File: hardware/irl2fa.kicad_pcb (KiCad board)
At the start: 2 copper layers, 80 x 34 mm, 52 parts, among them J1 FH34SRJ-24S, J3 TC2030-NL, Q1 AO3401A, Q2 AO3401A, Q3 Si1308EDL, Q4 AO3400A, Q5 VEMT2523SLX01, SW1 SKRHABE010, U1 STM32U083KCU6, U2 RV-3032-C7

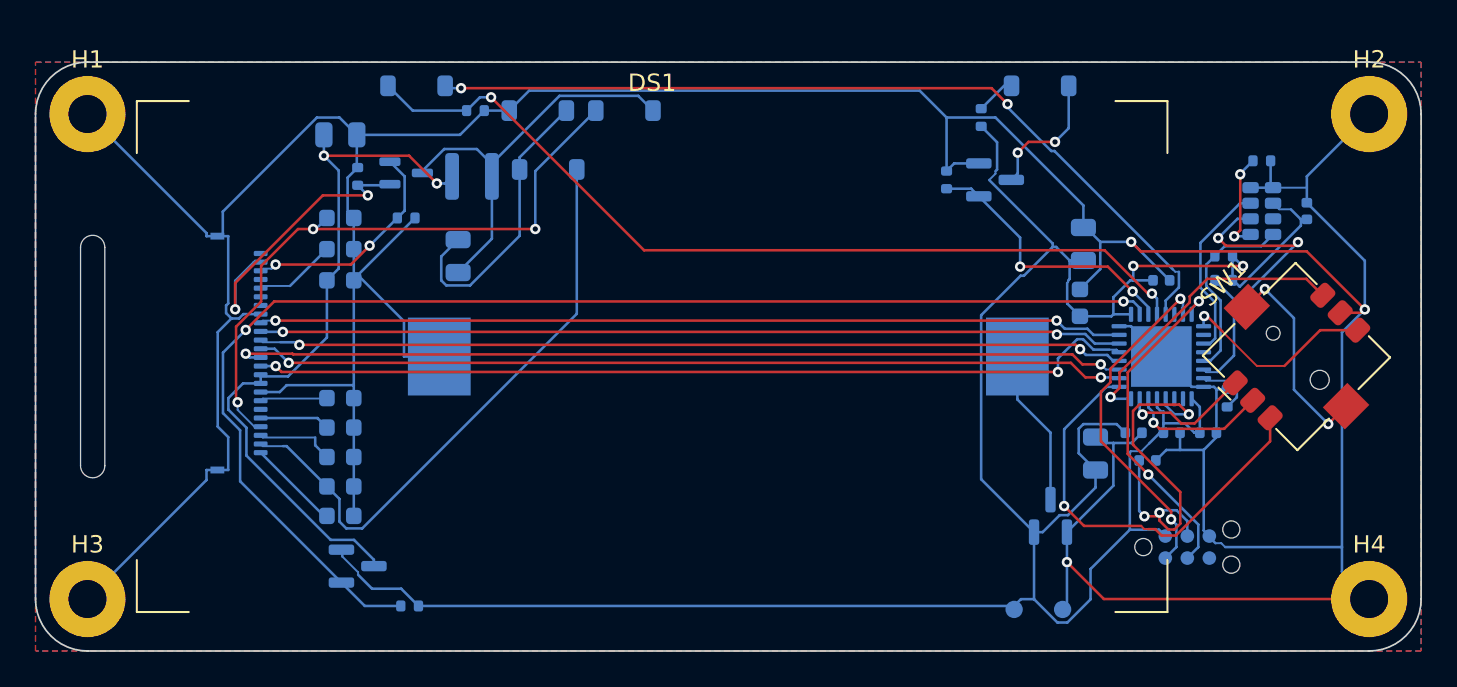
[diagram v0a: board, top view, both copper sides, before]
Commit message: Make the fob smaller: 80.9 x 34.9 x 11.0 mm case, 77 x 31 x 0.8 mm board
The 7.5 mm BS-24-B4AA016 holder set the case thickness. Replace it with
the MYOUNG MY-2450-01 CR2450 clip (LCSC C964845, 5.70 mm, 5355 in stock,
$0.17): a sprung plate over the cell, with a bare 12 mm ENIG pad under
it as the negative contact. Same cell, so the battery-life budget is
unchanged.

- Board 80 x 34 x 1.0 -> 77 x 31 x 0.8 mm, corner radius 2.6, holes at
  the corner centres. Glass 0.9 mm from the long edges, 0.4 mm clear of
  the case's screw bosses; joystick 1.2 mm from the glass.
- Case 83.9 x 37.9 x 13.0 -> 80.9 x 34.9 x 11.0 mm (keep-out 7.6 -> 5.8).
- New footprint and model for the clip, drawn from drawing MY-CP-0106.
  The courtyard is the union of plate, cell and pads. The SKRH courtyard
  now follows body and pads instead of their bounding box.
- The cell slides in from the bottom edge. Rule area: no vias under the
  cell. J1 keeps its FPC insertion offset on the thinner board.
- Re-placed and re-routed (Freerouting 2.5): ERC/DRC 0 errors,
  0 unconnected. Fab outputs, case STL/3MF, renders and docs regenerated.
- Case tests take the skin samples above and below the window from
  board.yaml rather than fixed coordinates.

Co-Authored-By: Claude Opus 5.5 <noreply@anthropic.com>
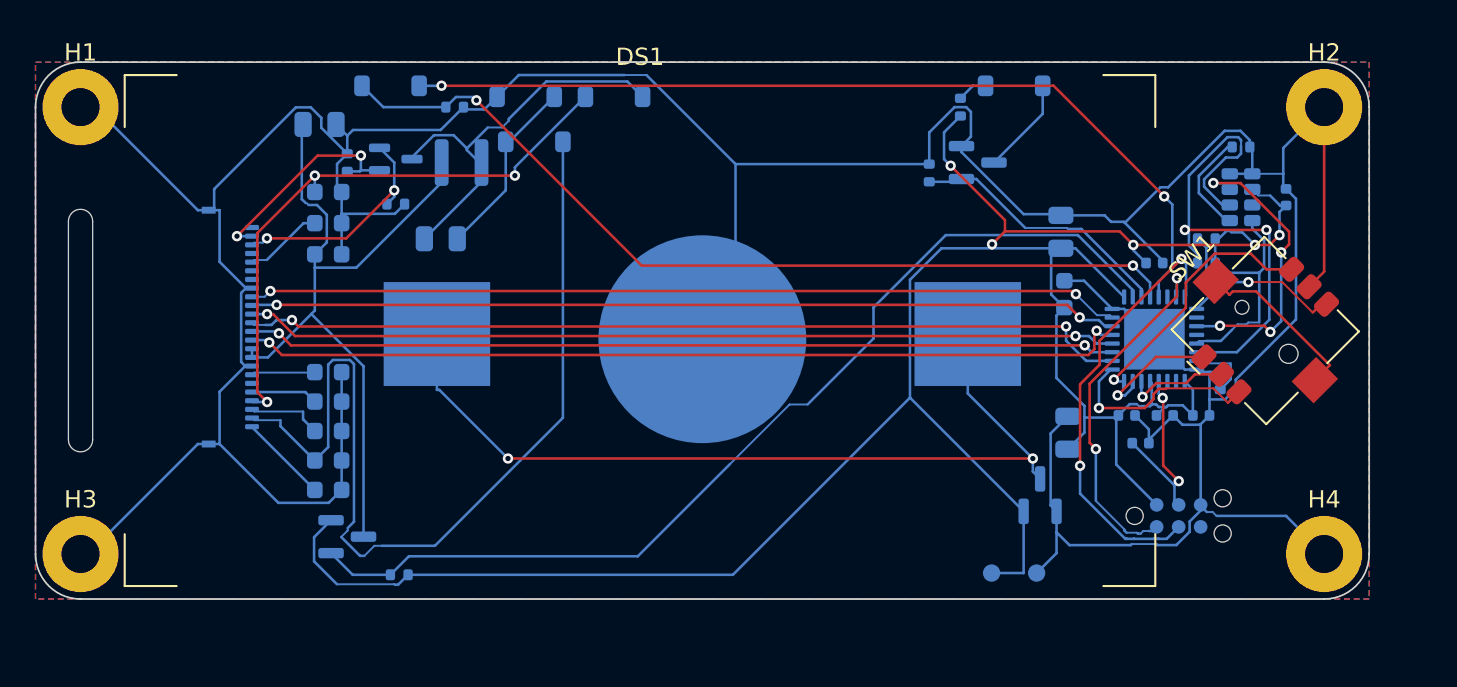
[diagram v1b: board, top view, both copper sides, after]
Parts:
- BT1: footprint irl2fa:BatteryHolder_MYOUNG_BS-24-B4AA016_CR2450 -> irl2fa:BatteryHolder_MYOUNG_MY-2450-01_CR2450
- moved H4 3.68 mm to (174.4, 128.4)
- moved H2 2.63 mm to (174.4, 102.6)
- moved H3 2.63 mm to (102.6, 128.4)
- moved TP2 2.58 mm to (157.8, 129.5)
- moved TP1 2.47 mm to (155.2, 129.5)
- moved SW1 2.34 mm to (171.0, 115.5)
- moved C2 2.00 mm to (159.6, 121.4)
- moved R5 1.90 mm to (121.0, 129.6)
- moved J3 1.87 mm to (166.0, 126.2)
- moved BT1 1.80 mm to (138.5, 116.0), turned to 180 degrees
- moved Q2 1.80 mm to (118.0, 127.4)
- moved D1 1.79 mm to (128.8, 104.6)
- moved C12 1.66 mm to (116.9, 107.5)
- moved C13 1.66 mm to (116.9, 109.3)
- moved C14 1.66 mm to (116.9, 111.1)
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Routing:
- net /VBAT_RAW: track 9.05 -> 49.4 mm, vias 0 -> 2
- net /GND: track 267.4 -> 246.3 mm, vias 3 -> 0
- net /EPD_PREVGL: track 34.5 -> 55.2 mm
- net /EPD_PWR_N: track 74.8 -> 57.7 mm, vias 2 -> 0
- net /JOY_C: track 24.8 -> 11.9 mm
- net /I2C_SDA: track 19.3 -> 30.3 mm
- net /NRST: track 22.2 -> 11.3 mm, vias 3 -> 2
- net /RTC_INT: track 10.5 -> 17.3 mm, vias 0 -> 4
- net /EPD_NEG: track 16.9 -> 10.6 mm
- net /SWCLK: track 19.4 -> 25.4 mm
- net /EPD_GDR: track 17.6 -> 12.7 mm
- net /I2C_SCL: track 11.1 -> 15.6 mm
- net /VBAT: track 141.0 -> 144.4 mm, vias 2 -> 5
- net /JOY_D: track 11.5 -> 9.07 mm
- net /EPD_PREVGH: track 36.7 -> 34.3 mm
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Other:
- board size 80 x 34 mm -> 77 x 31 mm

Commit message: Fix the silkscreen and turn the IR parts to face out through the top edge
Silkscreen: reference designators overlapped each other, sat on pads and ran
off the board edge, because silk_overlap, silk_over_copper and
silk_edge_clearance were only DRC warnings. They are errors now, and a new
gen_pcb.py --step silk places every label clear of pads, other silk, part
bodies, the coin cell and its insertion path, the FPC slot and the edge
(0.8 mm, 0.65 mm where that can't fit; hidden only where nothing fits: the
display, the booster diodes and inductor, and Q5). R3/R4 moved 0.3 mm clear
of U2's pin-1 mark, the clip's "+" moved to the contact away from C11, and
the IR parts' pin-1 bars stop short of the edge.

IR orientation: placing a part on the back mirrors it top to bottom, so D4
and Q5, placed at 0 deg, had their lenses facing into the board. Their pads
are symmetric, so ERC, DRC and the footprint checks all passed. They are now
at 180 deg (board re-routed, DRC clean), and test_orientation.py checks it.

Also: gen_pcb.py --step refresh (library footprint updates without
re-routing), hardware/tools/render_pcb.sh and `make renders`, new renders.

Co-Authored-By: Claude Opus 5.5 <noreply@anthropic.com>
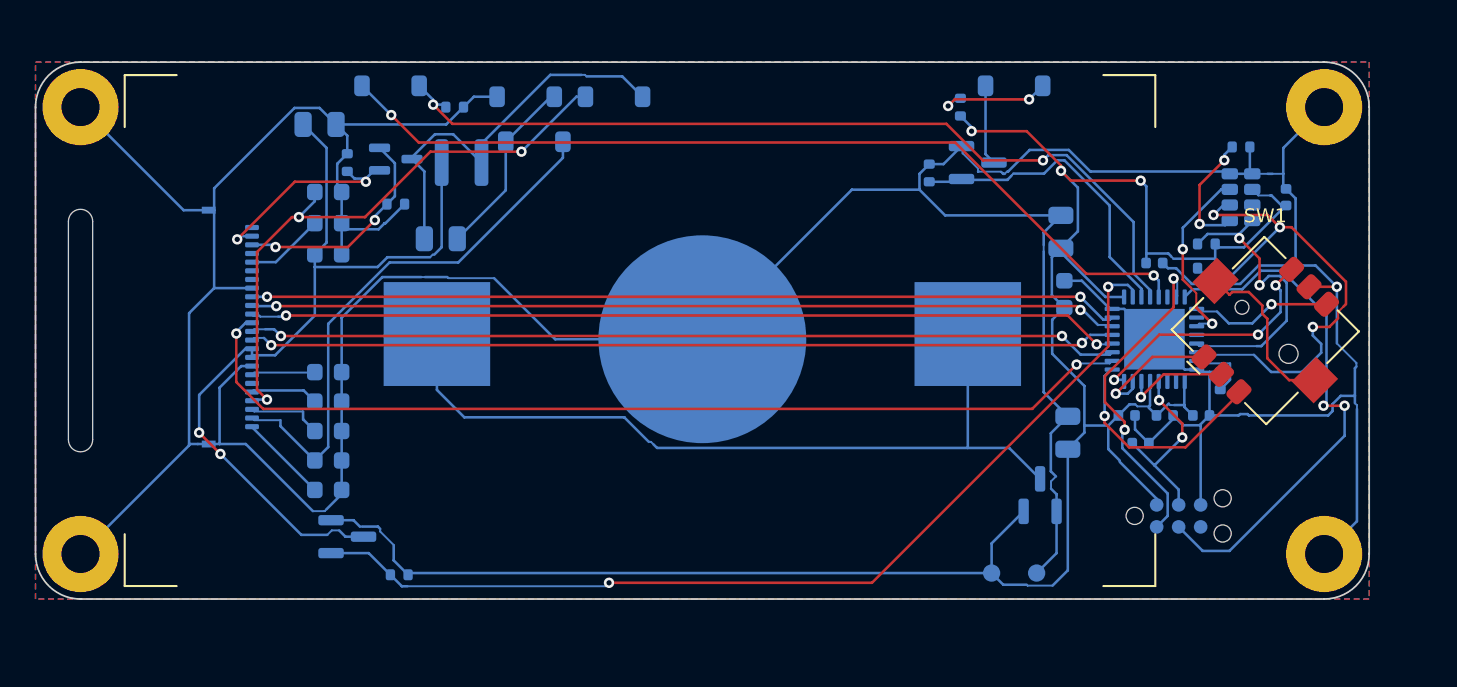
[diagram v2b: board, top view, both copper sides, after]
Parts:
- moved R4 0.30 mm to (167.6, 111.9)
- moved R3 0.30 mm to (167.6, 110.5)
- turned D4 to 180 degrees
- turned Q5 to 180 degrees
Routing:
- net /EPD_PREVGL: track 55.2 -> 31.5 mm
- net /GND: track 246.3 -> 266.9 mm, vias 0 -> 1
- net /VBAT: track 144.4 -> 126.7 mm, vias 5 -> 3
- net /RTC_INT: track 17.3 -> 10.8 mm, vias 4 -> 2
- net /VEPD: track 41.8 -> 48.2 mm, vias 0 -> 2
- net /SWCLK: track 25.4 -> 31.0 mm
- net /EPD_CS: track 51.3 -> 56.4 mm
- net /IR_LED_A: track 1.75 -> 6.83 mm, vias 0 -> 2
- net /IR_TX: track 15.4 -> 18.1 mm
- net /VBAT_RAW: track 49.4 -> 46.8 mm, vias 2 -> 0
- net /SWDIO: track 20.7 -> 19.0 mm
- net /I2C_SCL: track 15.6 -> 17.2 mm, vias 0 -> 2
- net /JOY_C: track 11.9 -> 13.0 mm
- net /EPD_SDI: track 51.2 -> 50.1 mm
- net /IR_RX: track 51.5 -> 50.4 mm
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
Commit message: WIP board fixes: parts, keep-outs, silkscreen, test pads, benches (board not yet routed)
Co-Authored-By: Claude Opus 5.5 <noreply@anthropic.com>
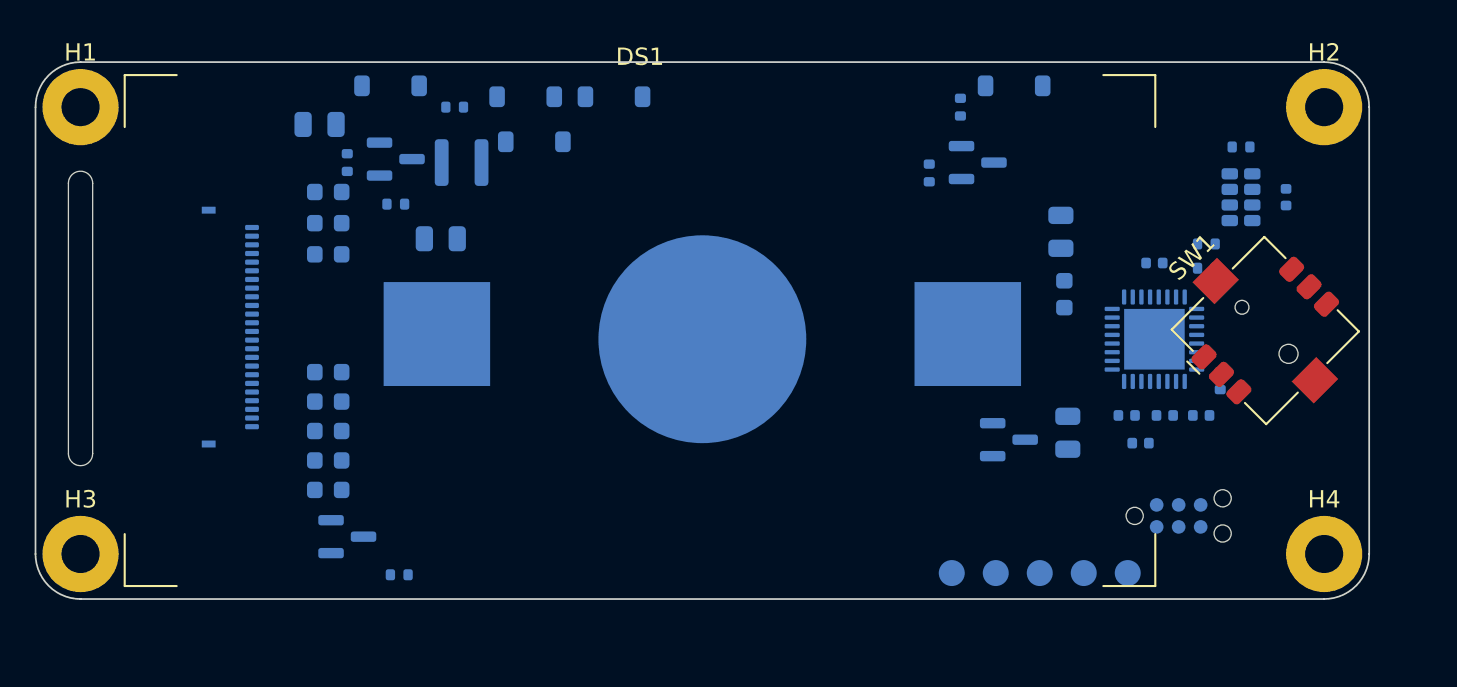
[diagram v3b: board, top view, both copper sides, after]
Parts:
- added TP3: SWDIO, TestPoint:TestPoint_Pad_D1.5mm, B.Cu at (158.0, 129.5)
- added TP4: SWCLK, TestPoint:TestPoint_Pad_D1.5mm, B.Cu at (160.5, 129.5)
- added TP5: NRST, TestPoint:TestPoint_Pad_D1.5mm, B.Cu at (163.1, 129.5)
- Q3: value Si1308EDL -> NX3008NBK; footprint Package_TO_SOT_SMD:SOT-323_SC-70 -> Package_TO_SOT_SMD:SOT-23
- Q5: value VEMT2523SLX01 -> VEMT2023SLX01; footprint irl2fa:PhotoTransistor_Vishay_VEMT2523SLX01_SideView -> irl2fa:PhotoTransistor_Vishay_VEMT2023SLX01_SideView
- R8: value 100 -> 68
- TP1, TP2: footprint TestPoint:TestPoint_Pad_D1.0mm -> TestPoint:TestPoint_Pad_D1.5mm
- moved TP2 4.90 mm to (152.9, 129.5)
- moved Q1 3.67 mm to (156.2, 121.8), turned to 0 degrees
- moved TP1 0.24 mm to (155.4, 129.5)
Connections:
- SW1 pad MP: unconnected-(SW1-PadMP) -> /GND
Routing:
- net /GND: track 266.9 -> 0.00 mm, vias 1 -> 0
- net /VBAT: track 126.7 -> 0.00 mm, vias 3 -> 0
- net /EPD_PWR_N: track 56.8 -> 0.00 mm, vias 2 -> 0
- net /EPD_CS: track 56.4 -> 0.00 mm, vias 2 -> 0
- net /IR_RX_PWR: track 51.6 -> 0.00 mm, vias 2 -> 0
- net /EPD_DC: track 50.5 -> 0.00 mm, vias 2 -> 0
- net /IR_RX: track 50.4 -> 0.00 mm, vias 2 -> 0
- net /EPD_SCK: track 50.4 -> 0.00 mm, vias 2 -> 0
- net /EPD_BUSY: track 50.3 -> 0.00 mm, vias 2 -> 0
- net /EPD_RST: track 50.2 -> 0.00 mm, vias 2 -> 0
- net /EPD_SDI: track 50.1 -> 0.00 mm, vias 2 -> 0
- net /VEPD: track 48.2 -> 0.00 mm, vias 2 -> 0
- net /VBAT_RAW: track 46.8 -> 0.00 mm
- net /EPD_PREVGH: track 34.2 -> 0.00 mm, vias 3 -> 0
- net /EPD_PREVGL: track 31.5 -> 0.00 mm
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- removed copper zone on B.Cu, net (none)
- removed copper zone on F.Cu, net (none)
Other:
- board text removed: "CERN-OHL-S-2.0"
- board text removed: "IRL2FA"
- board text removed: "v0.1 irl2fa.com"
